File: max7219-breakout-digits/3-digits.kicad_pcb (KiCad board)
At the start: 2 copper layers, 47.8 x 10.7 mm, 5 parts, among them J1 Conn_02x08_Odd_Even, U1 7Segment 3 digit common catho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

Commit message: MF Logo on correct positions, wrong link deleted
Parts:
- moved G2 25.9 mm to (122.2, 65.1)
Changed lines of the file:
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@@
 	(title_block
 		(title "7 Segment Display Module, 3 digits")
-		(date "2025-11")
-		(rev "V5.2")
+		(date "2025-12")
+		(rev "V6.0")
 		(company "MobiFlight")
 	)
@@
 	(footprint "MobiFlight:MobiFlight-Logo-Small"
 		(layer "B.Cu")
-		(at 96.27 64.23 180)
+		(at 122.18 65.14 180)
 		(property "Reference" "G2"
 			(at 0 0 0)

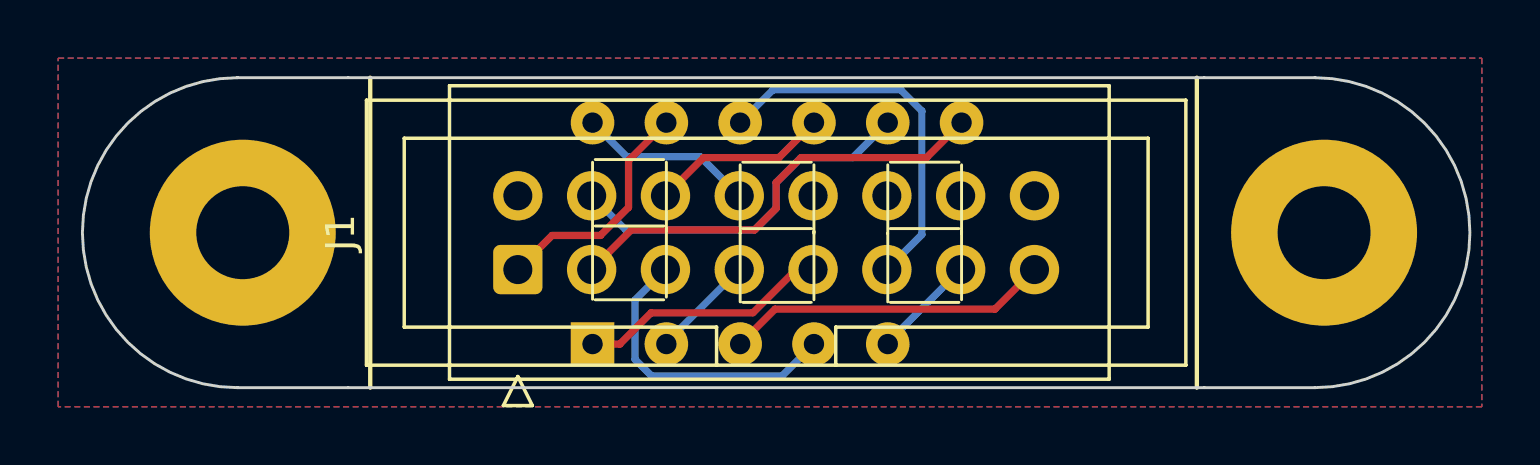
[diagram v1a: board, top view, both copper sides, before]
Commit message: fixed IDC connector on wrong side for 3 and 5 digit
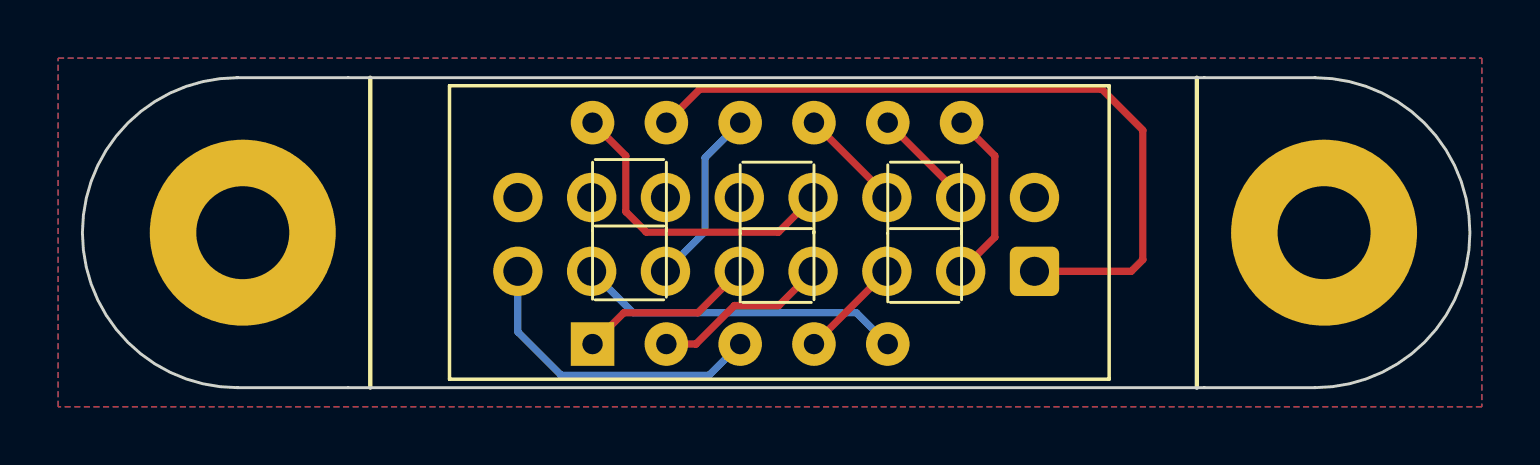
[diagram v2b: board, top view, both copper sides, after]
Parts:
- J1: moved to B.Cu
- moved J1 17.8 mm to (117.6, 65.3)
- moved G2 0.25 mm to (122.1, 65.4)
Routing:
- net /A: track 8.15 -> 25.8 mm
- net /B: track 15.3 -> 6.08 mm
- net /DIG0: track 12.7 -> 3.62 mm
- net /G: track 3.60 -> 11.2 mm
- net /C: track 10.4 -> 3.55 mm
- net /F: track 13.0 -> 6.18 mm
- net /DIG2: track 6.09 -> 10.8 mm
- net /E: track 8.65 -> 6.09 mm
- net /DIG1: track 6.15 -> 3.62 mm
- net /D: track 3.60 -> 6.09 mm

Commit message: slight movement of mounting holes to get full millimeters
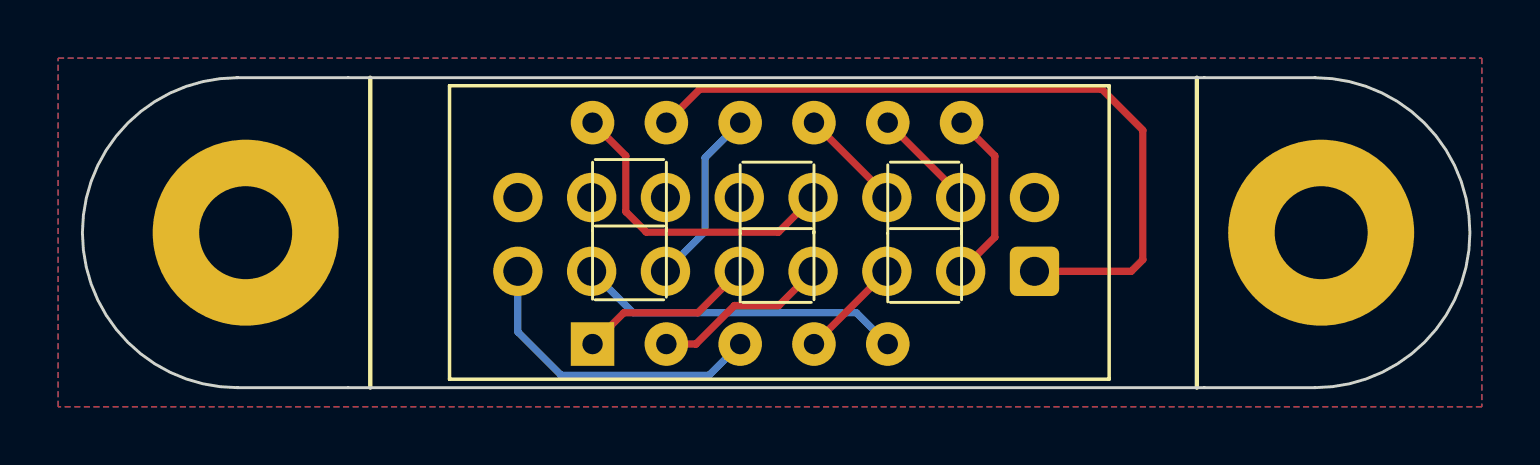
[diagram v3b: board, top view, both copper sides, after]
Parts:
- moved H1 0.10 mm to (90.5, 64.0)
- moved H2 0.10 mm to (127.5, 64.0)
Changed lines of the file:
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@@
 	(footprint "MountingHole:MountingHole_3.2mm_M3_Pad"
 		(layer "F.Cu")
-		(at 90.355107 64.008)
+		(at 90.455107 64.008)
 		(descr "Mounting Hole 3.2mm, M3, generated by kicad-footprint-generator mountinghole.py")
 		(tags "mountinghole M3")
@@
 	(footprint "MountingHole:MountingHole_3.2mm_M3_Pad"
 		(layer "F.Cu")
-		(at 127.568894 64.008)
+		(at 127.468894 64.008)
 		(descr "Mounting Hole 3.2mm, M3, generated by kicad-footprint-generator mountinghole.py")
 		(tags "mountinghole M3")
@@
 	)
 	(group ""
-		(members "6cce5ff6-859f-4c8a-817a-3f240ecd9819" "ee286778-0d6e-4304-8c5a-8bf6c46fde4f")
-	)
-	(group ""
